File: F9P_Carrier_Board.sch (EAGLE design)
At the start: 40 parts, among them J2 JTAG, J6 MICROMOD-2222-C, U5 AP7361C-33

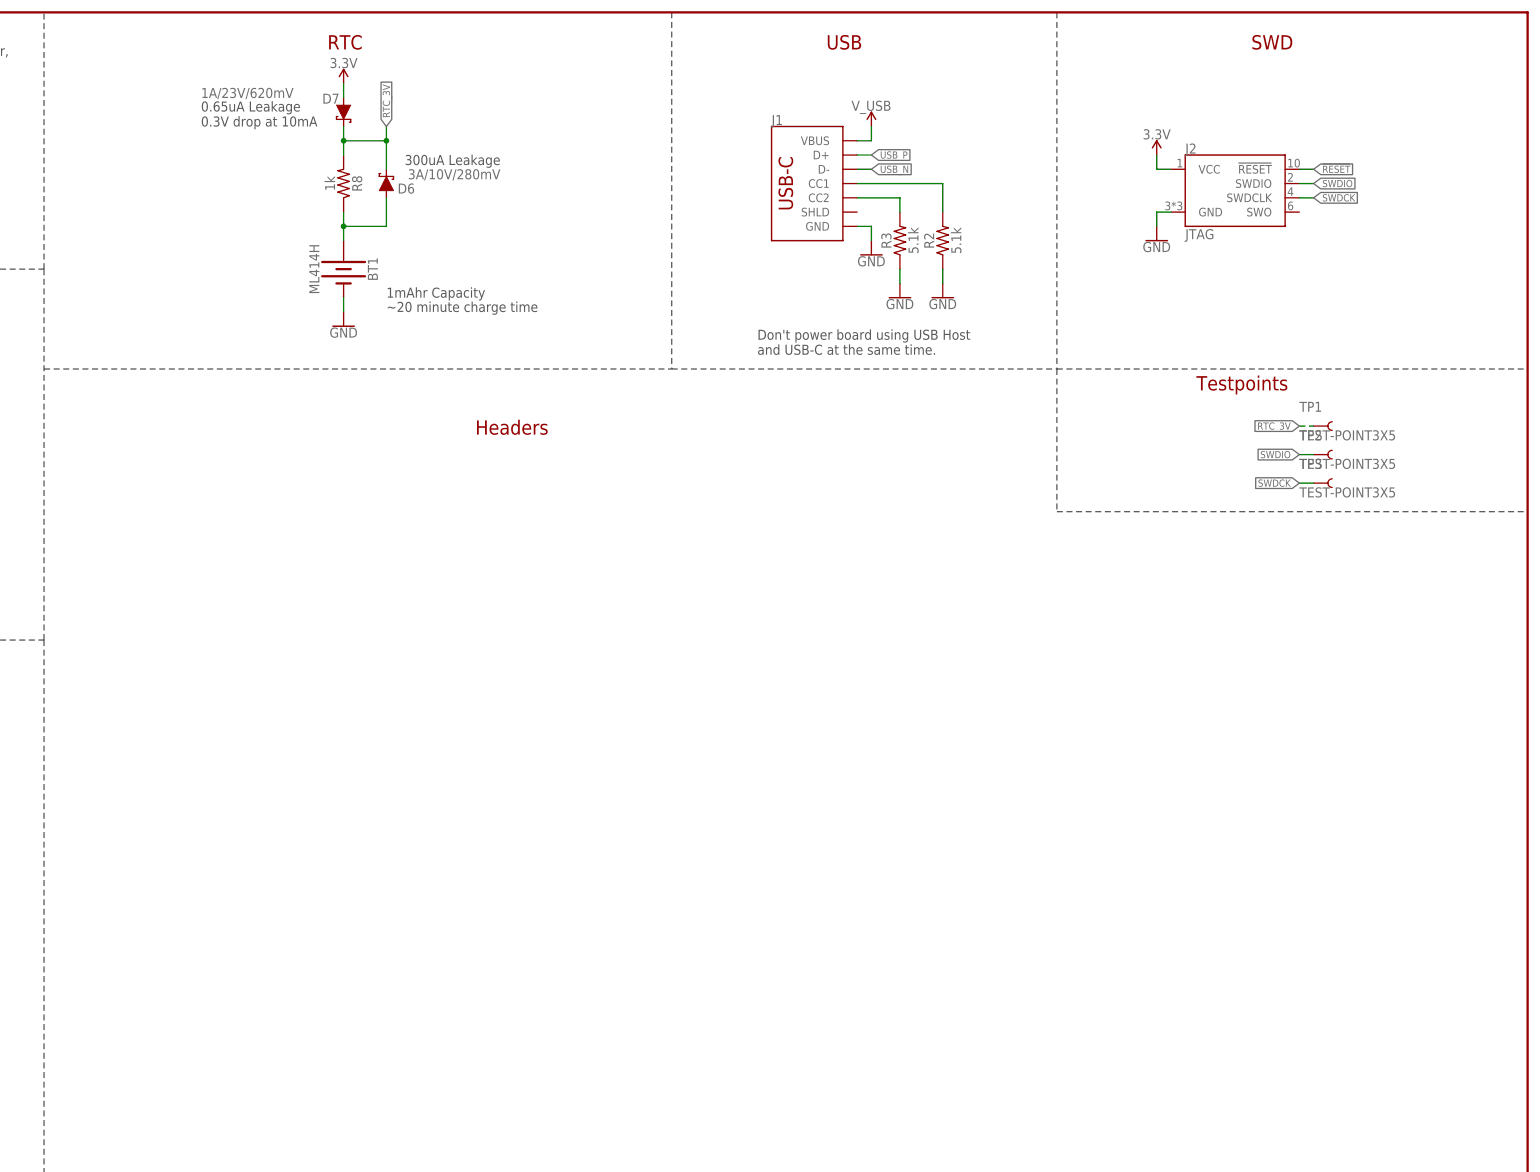
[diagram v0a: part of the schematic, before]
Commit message: Adds the F9R and the ESD protection diode
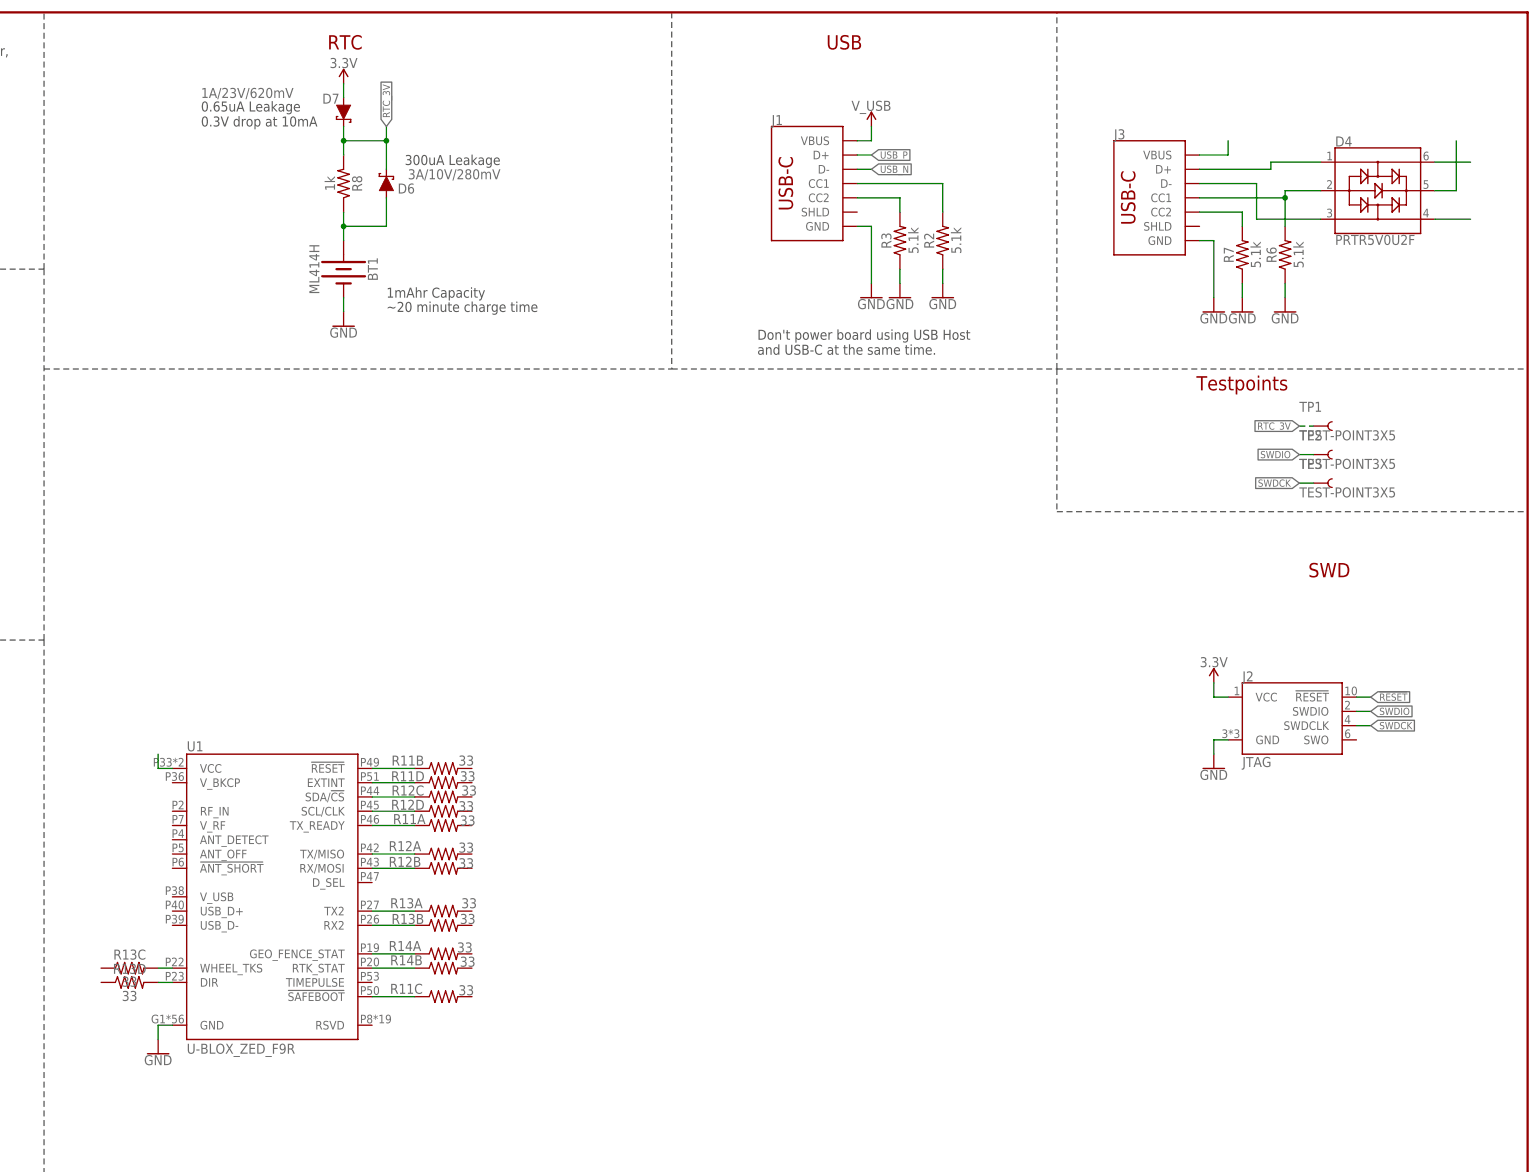
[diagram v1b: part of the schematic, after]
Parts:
- added D4: PRTR5V0U2F, SparkFun-IC-Power:PRTR5V0U2F
- added J3: (no value), SparkFun-Connectors:USB_C_2-LAYER_PADS
- added R11, R12, R13, R14: 33, SparkFun-Resistors:33OHM_RA-1206-1/16W-5%
- added R6, R7: 5.1k, SparkFun-Resistors:5.1KOHM5.1KOHM-0603-1/10W-1%
- added U1: U-BLOX_ZED_F9R, SparkFun-GPS:U-BLOX_ZED_F9R
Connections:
- new net N$12: D4.1, J3.D+
- new net N$13: D4.3, J3.D-
- new net N$15: R11B.1, U1.!RESET!
- new net N$16: R11D.1, U1.EXTINT
- new net N$17: D4.6
- new net N$18: D4.4
- new net N$19: R11A.1, U1.TX_READY
- new net N$20: R11C.1, U1.!SAFEBOOT!
- new net N$21: R12C.1, U1.SDA/!CS!
- new net N$22: R12D.1, U1.SCL/CLK
- new net N$23: R12A.1, U1.TX/MISO
- new net N$24: R12B.1, U1.RX/MOSI
- new net N$25: R13A.1, U1.TX2
- new net N$26: R13B.1, U1.RX2
- new net N$27: R13D.2, U1.DIR
- new net N$28: R13C.2, U1.WHEEL_TKS
- new net N$29: R14A.1, U1.GEO_FENCE_STAT
- new net N$30: R14B.1, U1.RTK_STAT
- new net N$31: U1.VCC
- new net N$6: D4.2, J3.CC1, R6.2
- new net N$7: J3.CC2, R7.2
- new net N$8: J3.VBUS
- new net N$9: D4.5
- net GND: now also J3.GND, R6.1, R7.1, U1.GND
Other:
- note removed: "Headers"
- moved on the sheet: J2

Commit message: Mostly finishes schematic
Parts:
- removed 3V3_LED, VIN_LED: JUMPER-SMT_2_NC_TRACE_SILK, SparkFun-Jumpers:JUMPER-SMT_2_NC_TRACE_SILK
- removed J2: JTAG, SparkFun-Connectors:CORTEX_JTAG_DEBUG_MINIMUM_PTH
- added 3V3, GEOF, PPS, RTK, VIN: JUMPER-SMT_2_NC_TRACE_SILK, SparkFun-Jumpers:JUMPER-SMT_2_NC_TRACE_SILK
- added BT2: ML414H_IV01E_BATTERY, SparkFun-Batteries:ML414H_IV01E_BATTERY
- added C3, C4: 0.1uF, SparkFun-Capacitors:0.1UF-0402T-6.3V-10%-X7R
- added C8: 47pF, SparkFun-Capacitors:47PF-0402-25V-5%-X7R
- added D10, D8, D9: BLUE, SparkFun-LED:LED-BLUE0603
- added D11: 0.5A/40V/420mV, SparkFun-DiscreteSemi:DIODE-SCHOTTKY-PMEG4005EJ
- added FB1: FERRITE_BEAD-120_OHM-0402T, SparkFun-Coils:FERRITE_BEAD-120_OHM-0402T
- added FD2, FD4: FIDUCIALUFIDUCIAL, SparkFun-Aesthetics:FIDUCIALUFIDUCIAL
- added H1, H2, H3, H4: STAND-OFFTIGHT, SparkFun-Hardware:STAND-OFFTIGHT
- added J10: (no value), SparkFun-Connectors:CONN_09NO_SILK
- added J4: U.FL, SparkFun-Connectors:U.FL2PIN
- added J5: QWIIC_RIGHT_ANGLE, SparkFun-Connectors:QWIIC_CONNECTORJS-1MM
- added J7: (no value), SparkFun-Connectors:CONN_08NO_SILK_DNP
- added J8: JTAG, SparkFun-Connectors:CORTEX_JTAG_DEBUG_MINIMUM_PTH
- added J9: (no value), SparkFun-Connectors:CONN_06NO_SILK_NO_POP
- added JP5: JUMPER-SMT_2_NO_SILK, SparkFun-Jumpers:JUMPER-SMT_2_NO_SILK
- added LOGO1: SFE_LOGO_NAME.1_INCH, SparkFun-Aesthetics:SFE_LOGO_NAME.1_INCH
- added R15, R16: 27OHM, SparkFun-Resistors:27OHM
- added R17: 33, SparkFun-Resistors:33OHM-0603-1/10W-1%
- added R19, R20, R21: 1KOHM-0402-1/16W-1%, SparkFun-Resistors:1KOHM-0402-1/16W-1%
- added R22: 100k, SparkFun-Resistors:100KOHM-0402T-1/16W-1%
- added R24: 3.3k, SparkFun-Resistors:3.3KOHM-0603-1/10W-1%
- U1: value U-BLOX_ZED_F9R -> U-BLOX_ZED-F9P; device SparkFun-GPS:U-BLOX_ZED_F9R -> SparkFun-GPS:U-BLOX_ZED-F9P
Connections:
- net SCL renamed SCL/SCK
- removed net !CS!: J6.SPI_!CS!
- removed net !CS1!/DAT3: J6.SPI_!CS1!/SDIO_DATA3
- removed net !RESET: J2.!RESET, J6.!RESET!, S1.2
- removed net A0: J6.A0
- removed net A1: J6.A1
- removed net CAN_RXI: J6.CAN-RX
- removed net CAN_TXO: J6.CAN-TX
- removed net CIPO: J6.SPI_SDI
- removed net CIPO1/DAT0: J6.SPI_SDI1/SDIO_DATA0
- removed net COPI: J6.SPI_SDO
- removed net COPI1: J6.SPI_SDO1/SDIO_CMD
- removed net CTS1: J6.CTS1
- removed net D0: J6.D0
- removed net D1: J6.D1/CAM_TRIG
- removed net DAT1: J6.SDIO_DATA1
- removed net DAT2: J6.SDIO_DATA2
- removed net G0: J6.G0/BUS0
- removed net G1: J6.G1/BUS1
- removed net G10/ADC_P: J6.G10/ADC_D+/CAM_VSYNC
- removed net G11: J6.G11
- removed net G2: J6.G2/BUS2
- removed net G3: J6.G3/BUS3
- removed net G4: J6.G4/BUS4
- removed net G5: J6.G5/BUS5
- removed net G6: J6.G6/BUS6
- removed net G7: J6.G7/BUS7
- removed net G8: J6.G8
- removed net G9/ADC_N: J6.G9/ADC_D-/CAM_HSYNC
- removed net I2S_CLK: J6.AUD_BCLK
- removed net I2S_SDI: J6.AUD_IN/CAM_PCLK
- removed net I2S_SDO: J6.AUD_OUT/CAM_MCLK
- removed net I2S_WS: J6.AUD_LRCLK
- removed net MCLK: J6.AUD_MCLK
- removed net N$31: U1.VCC
- removed net PWM0: J6.PWM0
- removed net PWM1: J6.PWM1
- removed net RTS1: J6.RTS1
- removed net RX1: J6.RX1
- removed net RX2: J6.RX2
- removed net SCK: J6.SPI_SCK
- removed net SCK1: J6.SPI_SCK1/SDIO_CLK
- removed net SCL1: J6.I2C_SCL1
- removed net SDA: J6.I2C_SDA
- removed net SDA1: J6.I2C_SDA1
- removed net TX1: J6.TX1
- removed net TX2: J6.TX2
- removed net USBHOST_N: J6.USBHOST_D-
- removed net USBHOST_P: J6.USBHOST_D+
- new net !RESET!: J6.!RESET!, J8.!RESET, S1.2
- new net !SAFEBOOT: J10.3
- new net !SAFEBOOT!: R11C.2
- new net !ZED_RESET!: J10.4, R11B.2
- new net D_SEL: JP5.1, U1.D_SEL
- new net GEOF_STAT: D10.A
- new net GEO_STAT: U1.GEO_STAT
- new net INT: J10.2, R11D.2
- new net N$32: D11.C, R24.2
- new net N$45: GEOF.2, R21.1
- new net N$46: D10.C, R21.2
- new net PPS: D8.A, J10.1, U1.TIMEPULSE
- new net RF_IN: FB1.1, J4.SIGNAL, U1.RF_IN
- new net RTK_STAT: D9.A, R14B.2
- new net RXI/SDI: J6.SPI_SDI, J6.TX1, J7.5, R12B.2
- new net RXI2: J6.TX2, J9.4, R13B.2
- new net SCL/CLK: J10.6, J5.4, J6.SPI_SCK, J7.7, R12D.2
- new net SDA/!CS!: J10.7, J5.3, J6.I2C_SDA, J6.SPI_!CS!, J7.4, R12C.2
- new net TXO/SDO: J6.RX1, J6.SPI_SDO, J7.6, R12A.2
- new net TXO2: J6.RX2, J9.5, R13A.2
- new net TX_READY: J10.5, R11A.2
- new net V_BATT: BT2.+, R24.1, U1.V_BKCP
- new net V_RF: R17.2, U1.V_RF
- new net ZED_USB_N: R16.2, U1.USB_D-
- new net ZED_USB_P: R15.2, U1.USB_D+
- net 3.3V: now also C3.1, C4.1, D11.A, D2.A, J10.8, J5.2, J7.3, J8.VCC, R22.2, U1.VCC, U1.V_USB; no longer J2.VCC, R1.2
- net GND: now also 3V3.2, BT2.-, C3.2, C4.2, C8.2, GEOF.1, J10.9, J4.GND, J5.1, J7.1, J7.8, J8.GND, J9.1, JP5.2, PPS.1, R22.1, RTK.1, VIN.2; no longer 3V3_LED.2, J2.GND, VIN_LED.2
- net N$1: now also D2.C, R1.2; no longer D2.A, R1.1
- net N$17: now also D4.4, R16.1; no longer D4.6
- net N$18: now also C8.1, FB1.2, R17.1; no longer D4.4
- net N$2: now also VIN.1; no longer D3.A
- net N$27: now also PPS.2, R19.1; no longer R13D.2, U1.DIR
- net N$28: now also D8.C, R19.2; no longer R13C.2, U1.WHEEL_TKS
- net N$29: now also D9.C, R20.2; no longer R14A.1, U1.GEO_FENCE_STAT
- net N$3: now also 3V3.1, R1.1; no longer 3V3_LED.1, D2.C
- net N$4: now also R4.2; no longer VIN_LED.1
- net N$8: now also R20.1, RTK.2; no longer J3.VBUS
- net N$9: now also D4.6, R15.1; no longer D4.5
- net SWDCK: now also J8.SWDCLK; no longer J2.SWDCLK
- net SWDIO: now also J8.SWDIO; no longer J2.SWDIO
- net VIN: now also D3.A, D4.5, J1.VBUS, J3.VBUS, J7.2; no longer R4.2
- net V_USB: no longer J1.VBUS
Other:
- note added: "*Battery Initial Charge: 2.3-2.8V *Intial Battery Capacity (maH): 800mAH or Greater *Battery Charge Rate: 1mA MAX *Voff: 2.0V *72 hours charge time from 2.0-3.1V"
- note added: "1k"
- note added: "Antenna"
- note added: "GPS Module ZED-F9P"
- note added: "Headers"
- note added: "USB Power and Program Processor Board"
- note added: "ZED-F9P Backup Battery"
- note added: "ZED-F9P USB (u-center)"
- note added: "v10"
- note removed: "Don't power board using USB Host and USB-C at the same time."
- note removed: "USB"
- note removed: "v11"
- moved on the sheet: BT1, D2, D3, D4, D6, D7, EN, H5, J1, J3, J6, R1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
